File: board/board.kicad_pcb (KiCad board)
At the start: 2 copper layers, 203 x 96 mm, 49 parts, among them U1 Seeed Studio XIAO SAMD21

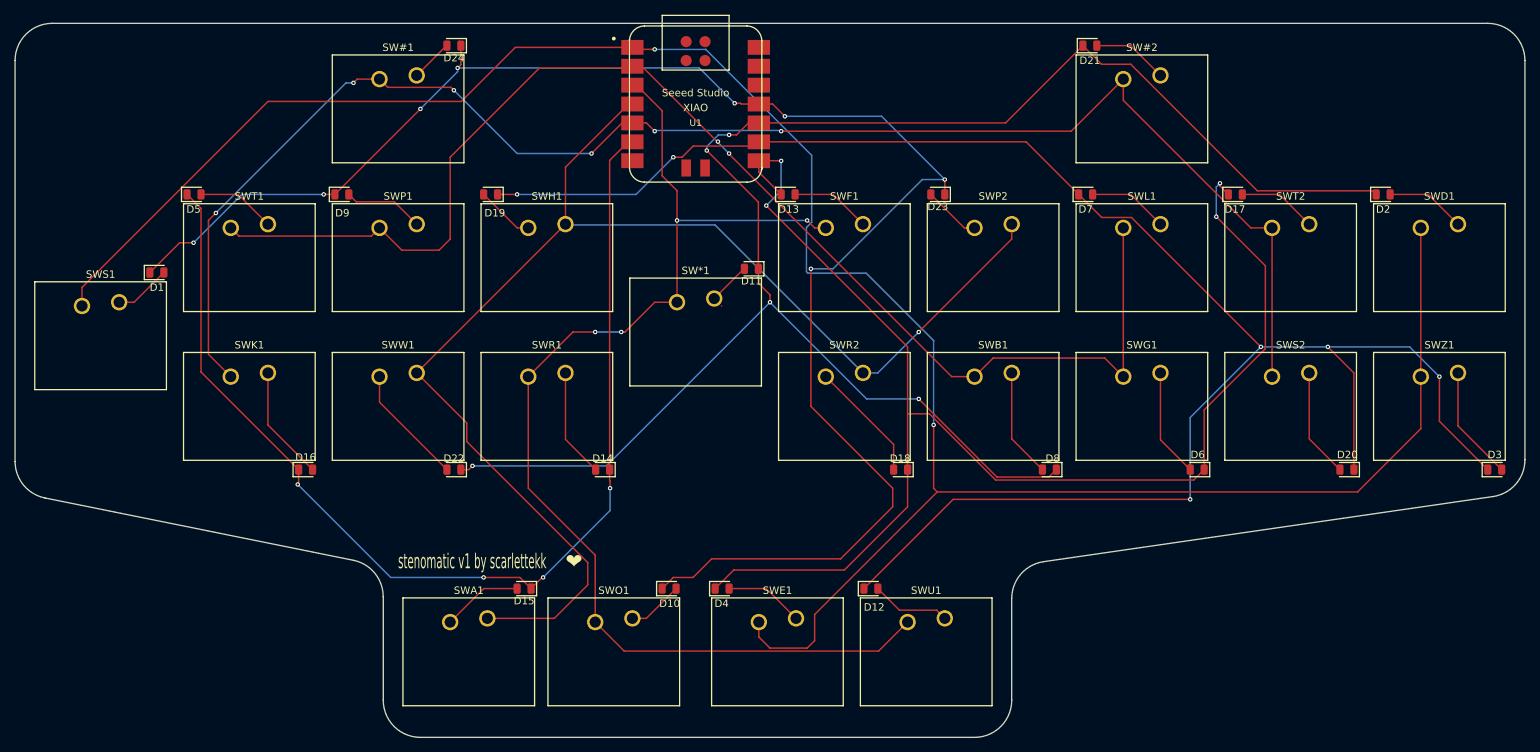
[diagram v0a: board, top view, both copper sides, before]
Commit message: switch to THT diodes for ease of installation
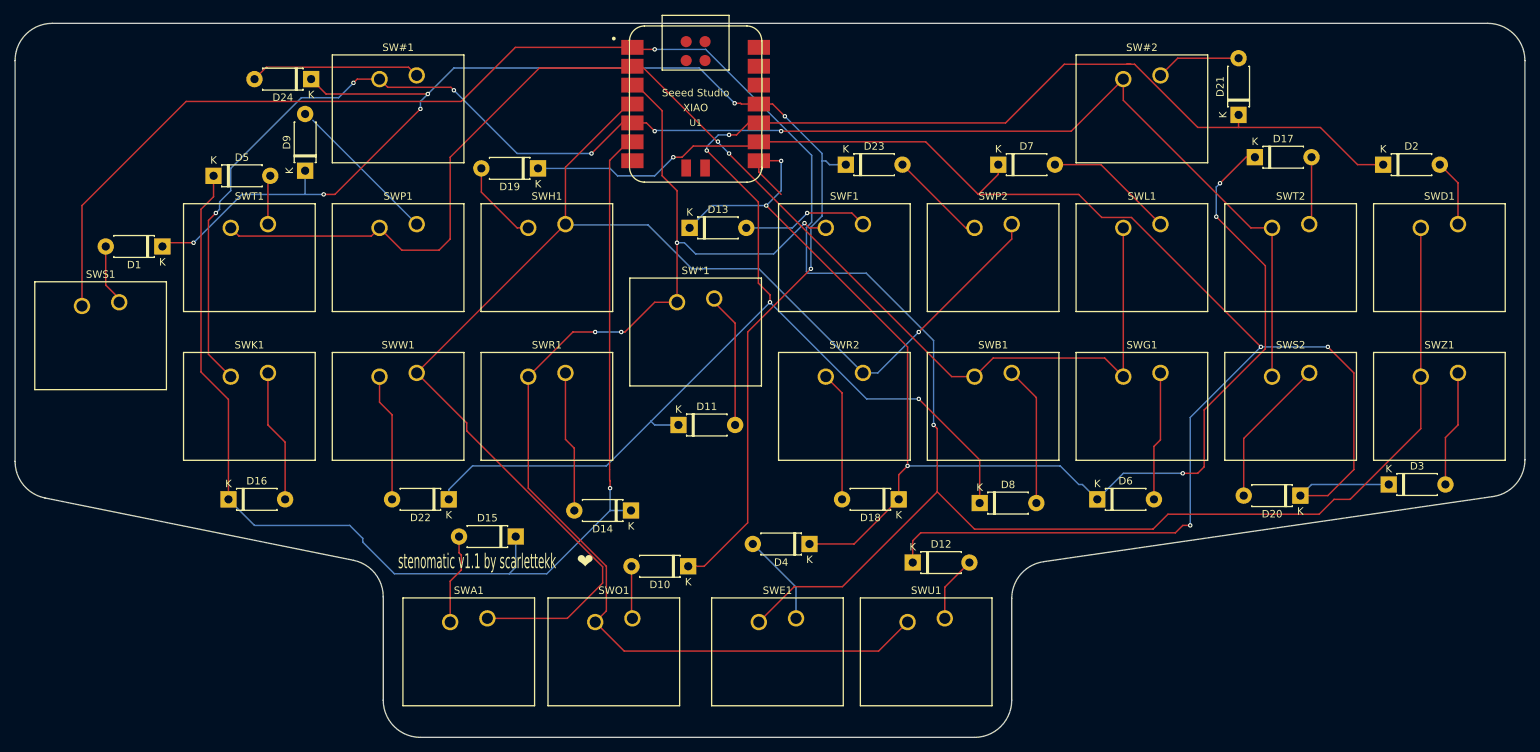
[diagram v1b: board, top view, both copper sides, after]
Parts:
- D1, D10, D11, D12, D13, D14, D15, D16, D17, D18, D19, D2, D20, D21, D22, D23, D24, D3, D4, D5, D6, D7, D8, D9: footprint Diode_SMD:D_0805_2012Metric -> Diode_THT:D_DO-41_SOD81_P7.62mm_Horizontal
- moved D11 23.2 mm to (126.7, 87.0), turned to 0 degrees
- moved D21 22.1 mm to (202.0, 45.3), turned to 90 degrees
- moved D24 19.7 mm to (77.3, 40.5)
- moved D3 14.4 mm to (222.2, 95.0)
- moved D6 14.0 mm to (183.0, 97.0), turned to 0 degrees
- moved D13 14.0 mm to (128.2, 60.5)
- moved D4 13.2 mm to (144.3, 103.0), turned to 180 degrees
- moved D23 13.0 mm to (149.2, 52.0), turned to 0 degrees
- moved D7 12.4 mm to (169.7, 52.0)
- moved D16 11.1 mm to (66.2, 97.0)
- moved D8 10.4 mm to (167.2, 97.5), turned to 0 degrees
- moved D19 7.27 mm to (107.8, 52.5)
- moved D20 7.17 mm to (210.3, 96.5)
- moved D15 7.09 mm to (104.8, 102.0)
- moved D14 6.69 mm to (120.3, 98.5)
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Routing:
- net Net-(D1-K): track 225.0 -> 191.3 mm, vias 8 -> 7
- net Net-(D24-A): track 5.72 -> 22.9 mm
- net Net-(D12-K): track 249.1 -> 233.2 mm, vias 6 -> 4
- net Net-(D14-K): track 148.6 -> 164.4 mm, vias 4 -> 1
- net Net-(D11-A): track 5.72 -> 18.2 mm
- net Net-(D9-A): track 10.8 -> 19.8 mm
- net Net-(D7-A): track 10.8 -> 17.5 mm
- net Net-(D13-A): track 10.8 -> 17.1 mm, vias 0 -> 1
- net Net-(D23-A): track 7.74 -> 13.2 mm
- net Net-(D20-A): track 14.7 -> 20.1 mm
- net Net-(U1-PA02_A0_D0): track 310.3 -> 314.8 mm
- net Net-(D14-A): track 14.7 -> 19.0 mm
- net Net-(D8-A): track 14.7 -> 18.9 mm
- net Net-(D5-A): track 10.7 -> 6.63 mm
- net Net-(D19-A): track 7.86 -> 11.5 mm
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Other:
- board text added: "stenomatic v1.1 by scarlettekk"
- board text removed: "stenomatic v1 by scarlettekk"

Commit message: missing trace
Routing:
- net Net-(D9-A): track 19.8 -> 40.9 mm

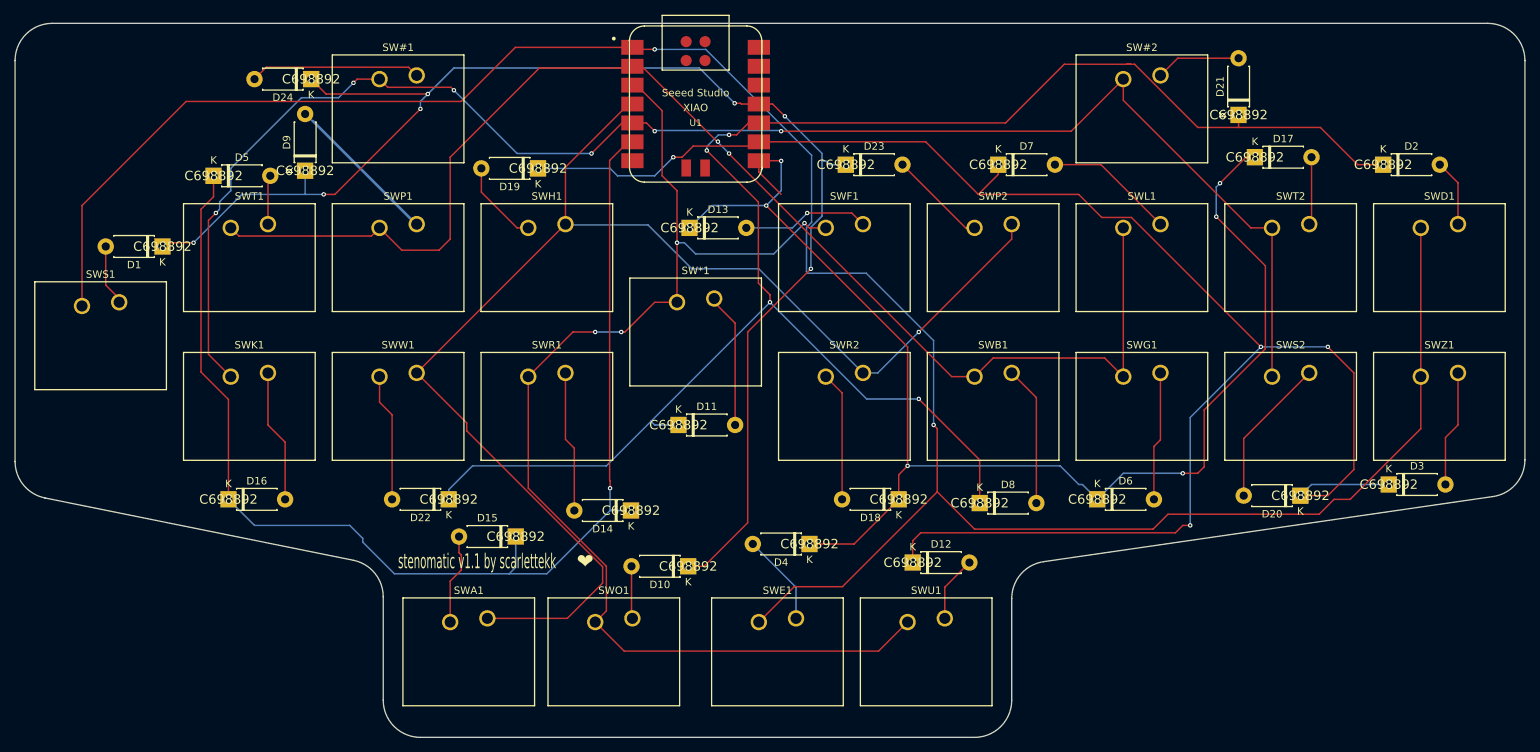
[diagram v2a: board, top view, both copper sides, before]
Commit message: remove spurious silkscreen
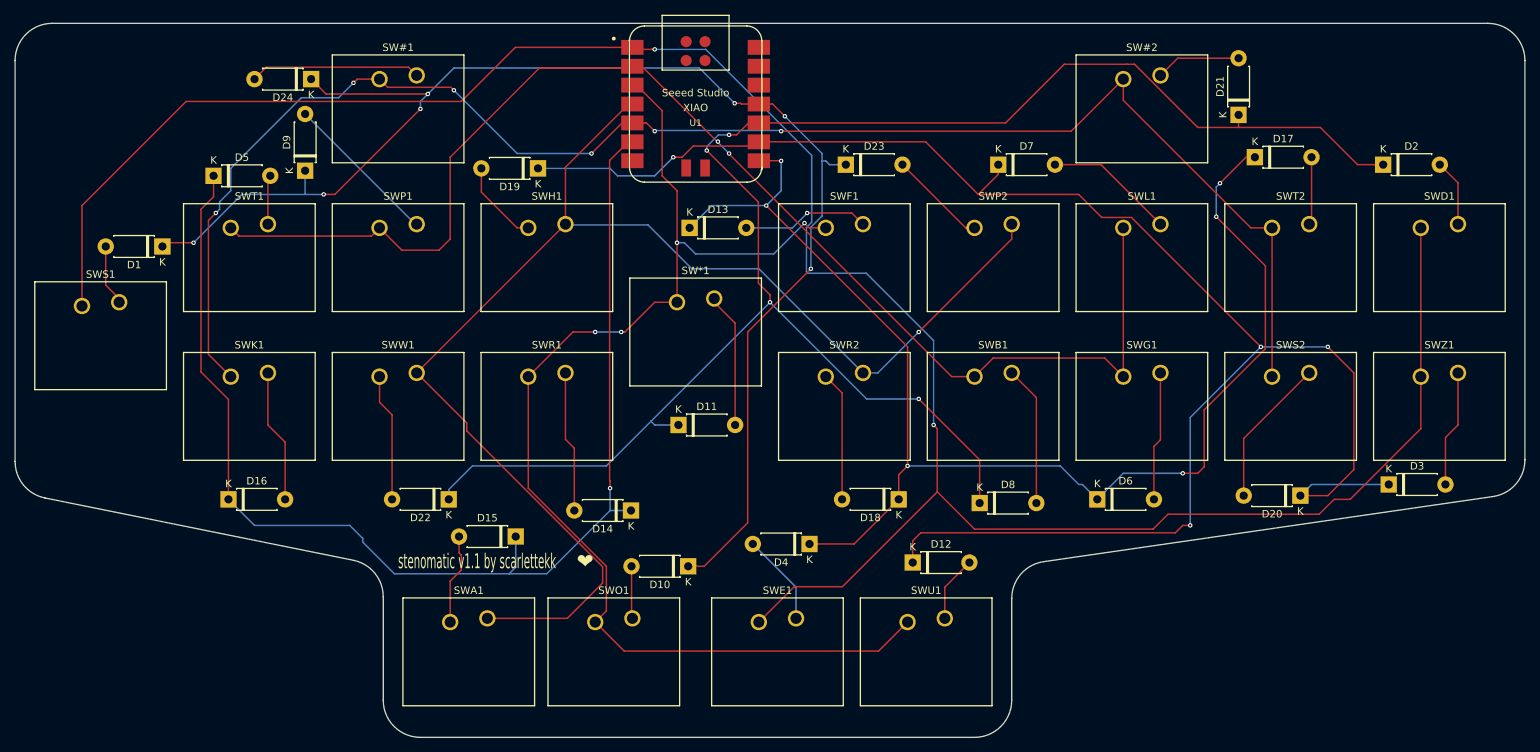
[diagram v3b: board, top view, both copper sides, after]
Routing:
- net Net-(D9-A): track 40.9 -> 21.1 mm
- net Net-(D13-K): track 183.7 -> 177.9 mm
- net Net-(D11-K): track 229.4 -> 228.9 mm
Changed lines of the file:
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@@
 			(at 0 0 0)
 			(layer "F.SilkS")
+			(hide yes)
 			(effects
 				(font
@@
 			(at 0 0 0)
 			(layer "F.SilkS")
+			(hide yes)
 			(effects
 				(font
@@
 			(at 0 0 0)
 			(layer "F.SilkS")
+			(hide yes)
 			(effects
 				(font
@@
 			(at 0 0 0)
 			(layer "F.SilkS")
+			(hide yes)
 			(effects
 				(font
@@
 			(at 0 0 0)
 			(layer "F.SilkS")
+			(hide yes)
 			(effects
 				(font
@@
 			(at 0 0 0)
 			(layer "F.SilkS")
+			(hide yes)
 			(effects
 				(font
@@
 			(at 0 0 0)
 			(layer "F.SilkS")
+			(hide yes)
 			(effects
 				(font
@@
 			(at 0 0 0)
 			(layer "F.SilkS")
+			(hide yes)
 			(effects
 				(font
@@
 			(at 0 0 0)
 			(layer "F.SilkS")
+			(hide yes)
 			(effects
 				(font
@@
 			(at 0 0 0)
 			(layer "F.SilkS")
+			(hide yes)
 			(effects
 				(font
@@
 			(at 0 0 0)
 			(layer "F.SilkS")
+			(hide yes)
 			(effects
 				(font
@@
 			(at 0 0 0)
 			(layer "F.SilkS")
+			(hide yes)
 			(effects
 				(font
@@
 			(at 0 0 0)
 			(layer "F.SilkS")
+			(hide yes)
 			(effects
 				(font
@@
 			(at 0 0 0)
 			(layer "F.SilkS")
+			(hide yes)
 			(effects
 				(font
@@
 			(at 0 0 0)
 			(layer "F.SilkS")
+			(hide yes)
 			(effects
 				(font
@@
 			(at 0 0 0)
 			(layer "F.SilkS")
+			(hide yes)
 			(effects
 				(font
@@
 			(at 0 0 0)
 			(layer "F.SilkS")
+			(hide yes)
 			(effects
 				(font
@@
 			(at 0 0 0)
 			(layer "F.SilkS")
+			(hide yes)
 			(effects
 				(font
@@
 			(at 0 0 0)
 			(layer "F.SilkS")
+			(hide yes)
 			(effects
 				(font
@@
 			(at 0 0 0)
 			(layer "F.SilkS")
+			(hide yes)
 			(effects
 				(font
@@
 			(at 0 0 0)
 			(layer "F.SilkS")
+			(hide yes)
 			(effects
 				(font
@@
 			(at 0 0 0)
 			(layer "F.SilkS")
+			(hide yes)
 			(effects
 				(font
@@
 			(at 0 0 0)
 			(layer "F.SilkS")
+			(hide yes)
 			(effects
 				(font
@@
 			(at 0 0 0)
 			(layer "F.SilkS")
+			(hide yes)
 			(effects
 				(font
@@
 	)
 	(segment
-		(start 187.5 38.5)
-		(end 187 38.5)
-		(width 0.2)
-		(layer "F.Cu")
-		(net 13)
-	)
-	(segment
 		(start 133.5 48)
 		(end 134.5 48)
@@
 	)
 	(segment
-		(start 137.5 53)
-		(end 140.5 56)
-		(width 0.2)
-		(layer "F.Cu")
-		(net 18)
-	)
-	(segment
 		(start 197.375 84.973529)
 		(end 205.6 76.748529)
@@
 	)
 	(segment
-		(start 137.5 51.47)
-		(end 137.5 53)
-		(width 0.2)
-		(layer "F.Cu")
-		(net 18)
-	)
-	(segment
 		(start 144.31 103)
 		(end 150.31 103)
@@
 	)
 	(segment
-		(start 91.5 60)
-		(end 77.532843 46.032843)
-		(width 0.2)
-		(layer "B.Cu")
-		(net 24)
-	)
-	(segment

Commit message: mounting holes
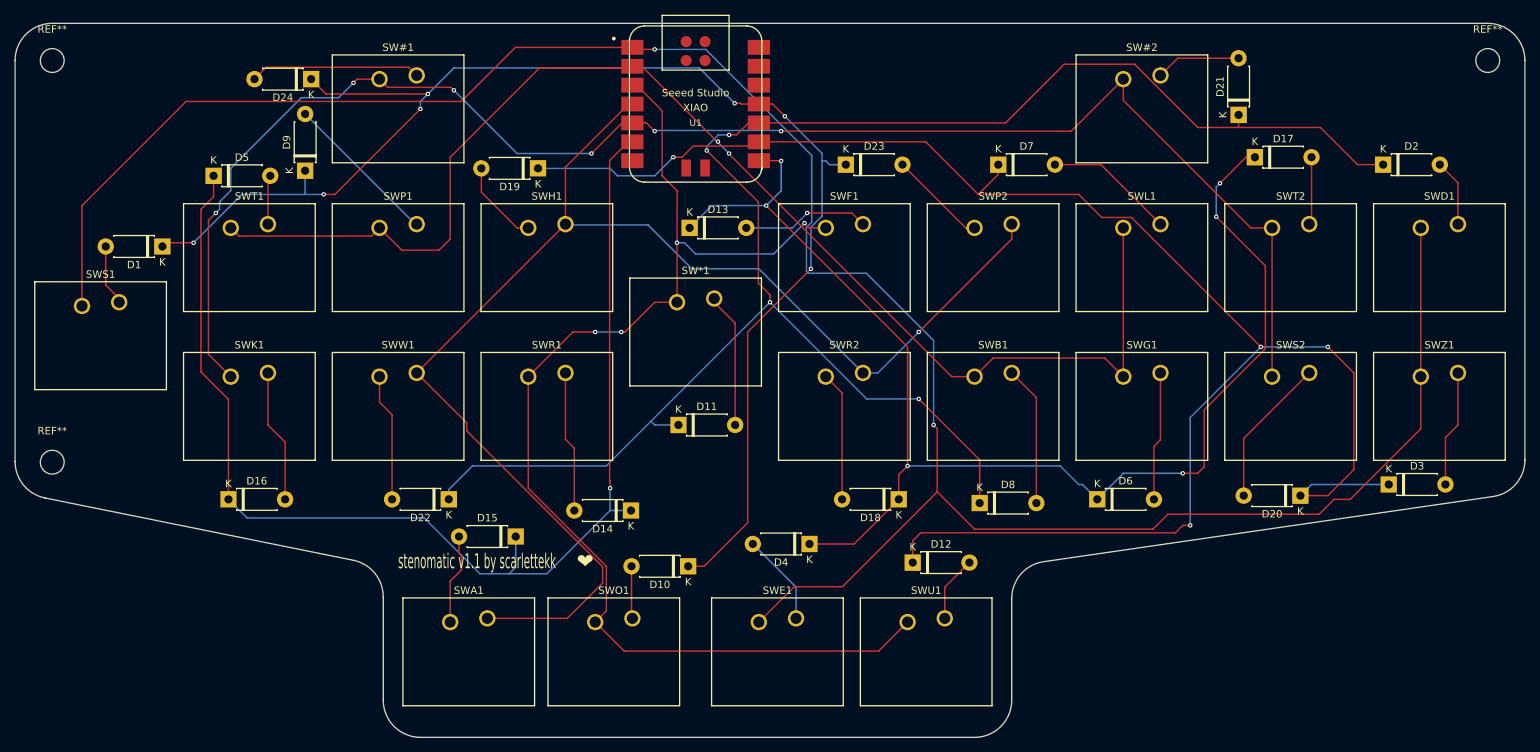
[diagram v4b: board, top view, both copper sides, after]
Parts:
- added REF**: MountingHole_3.2mm_M3, MountingHole:MountingHole_3.2mm_M3, F.Cu at (42.5, 92.0)
- added REF**: MountingHole_3.2mm_M3, MountingHole:MountingHole_3.2mm_M3, F.Cu at (235.5, 38.0)
- added REF**: MountingHole_3.2mm_M3, MountingHole:MountingHole_3.2mm_M3, F.Cu at (42.5, 38.0)

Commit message: add firmware, switch to choc keys, rewire (v2)
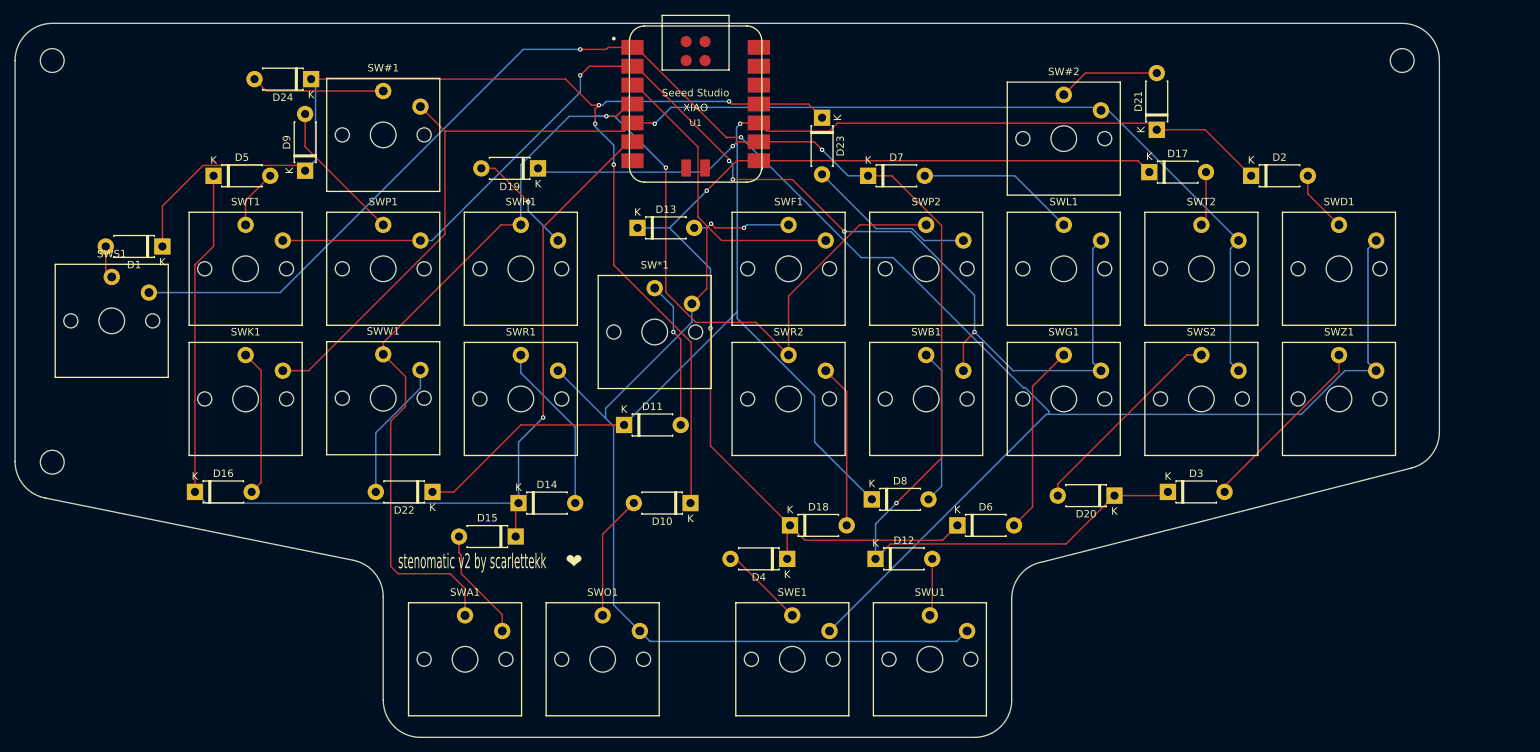
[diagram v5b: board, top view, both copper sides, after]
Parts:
- SW#1, SW#2, SWA1, SWB1, SWD1, SWE1, SWF1, SWG1, SWH1, SWK1, SWL1, SWO1, SWP1, SWP2, SWR1, SWR2, SWS2, SWT1, SWT2, SWU1, SWW1, SWZ1: footprint Button_Switch_Keyboard:SW_Matias_1.00u -> Switch_Keyboard_Kailh:SW_Kailh_Choc_V1_1.00u
- SW*1, SWS1: footprint Button_Switch_Keyboard:SW_Matias_1.00u -> Switch_Keyboard_Kailh:SW_Kailh_Choc_V1_2.00u_90deg
- moved D3 29.7 mm to (192.5, 96.0)
- moved D20 25.0 mm to (185.3, 96.5)
- moved D6 19.1 mm to (164.2, 100.5)
- moved D2 17.8 mm to (203.7, 53.5)
- moved D7 17.6 mm to (152.2, 53.5)
- moved SWD1 17.1 mm to (215.5, 66.0)
- moved SWZ1 16.4 mm to (215.5, 83.5)
- moved SWT2 15.7 mm to (197.0, 66.0)
- moved SW#2 15.5 mm to (178.5, 48.5)
- moved D14 15.2 mm to (105.2, 97.5), turned to 0 degrees
- moved D18 15.0 mm to (141.7, 100.5), turned to 0 degrees
- moved SWS2 14.9 mm to (197.0, 83.5)
- moved D8 14.5 mm to (152.7, 97.0)
- moved D17 14.3 mm to (190.0, 53.0)
- moved SWL1 14.3 mm to (178.5, 66.0)
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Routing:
- net Net-(D12-K): track 233.2 -> 152.7 mm, vias 4 -> 3
- net Net-(U1-P26_A0_D0): track 314.8 -> 261.8 mm
- net Net-(D11-K): track 228.9 -> 181.8 mm, vias 4 -> 1
- net Net-(U1-P6_SDA_D4): track 214.7 -> 181.9 mm, vias 6 -> 1
- net Net-(D13-K): track 177.9 -> 148.7 mm, vias 6 -> 2
- net Net-(D1-K): track 191.3 -> 170.6 mm, vias 7 -> 4
- net Net-(D14-K): track 164.1 -> 147.5 mm
- net Net-(U1-P27_A1_D1): track 178.3 -> 166.4 mm, vias 2 -> 5
- net Net-(D10-A): track 7.05 -> 16.8 mm
- net Net-(D23-A): track 13.2 -> 22.7 mm
- net Net-(D3-A): track 15.7 -> 24.8 mm
- net Net-(D6-A): track 17.4 -> 25.7 mm
- net Net-(D20-A): track 20.1 -> 28.0 mm
- net Net-(U1-P28_A2_D2): track 161.9 -> 156.4 mm, vias 4 -> 0
- net Net-(D24-A): track 22.9 -> 18.0 mm
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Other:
- board size 203 x 96 mm -> 191.5 x 96 mm
- board text added: "stenomatic v2 by scarlettekk"
- board text removed: "stenomatic v1.1 by scarlettekk"
